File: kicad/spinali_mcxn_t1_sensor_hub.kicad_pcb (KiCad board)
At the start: 6 copper layers, 45 x 46 mm, 199 parts, among them J1 5055780421, J2 USB4105-GF-A, J3 CAN0A, J4 CAN0B, J5 Debug, J6 CAN1A, J7 CAN1B, J8 DF40TC(3.0)-50DP-0.4V(51), J9 DF40TC(3.0)-50DP-0.4V(51), Q1 BUK6D56-60EX, SW1 SW_SPST, U1 LM74700, U10 BMM350, U11 BMP581, U12 TJA1462ATK, U13 TJA1462ATK, U14 SK9822-EC20, U15 TJA1103AHN, U2 NX5P3363UKZ, U3 LM5160DNTJ, U4 NX5P3363UKZ, U5 MIC5504-1.8YMT, U6 MPM3811GG-Z, U7 MCXN947VDFT, U8 PCMF1USB3SZ, U9 ICM-45686, Y1 24MHz, Y2 32.768kHz, Y3 25MHz

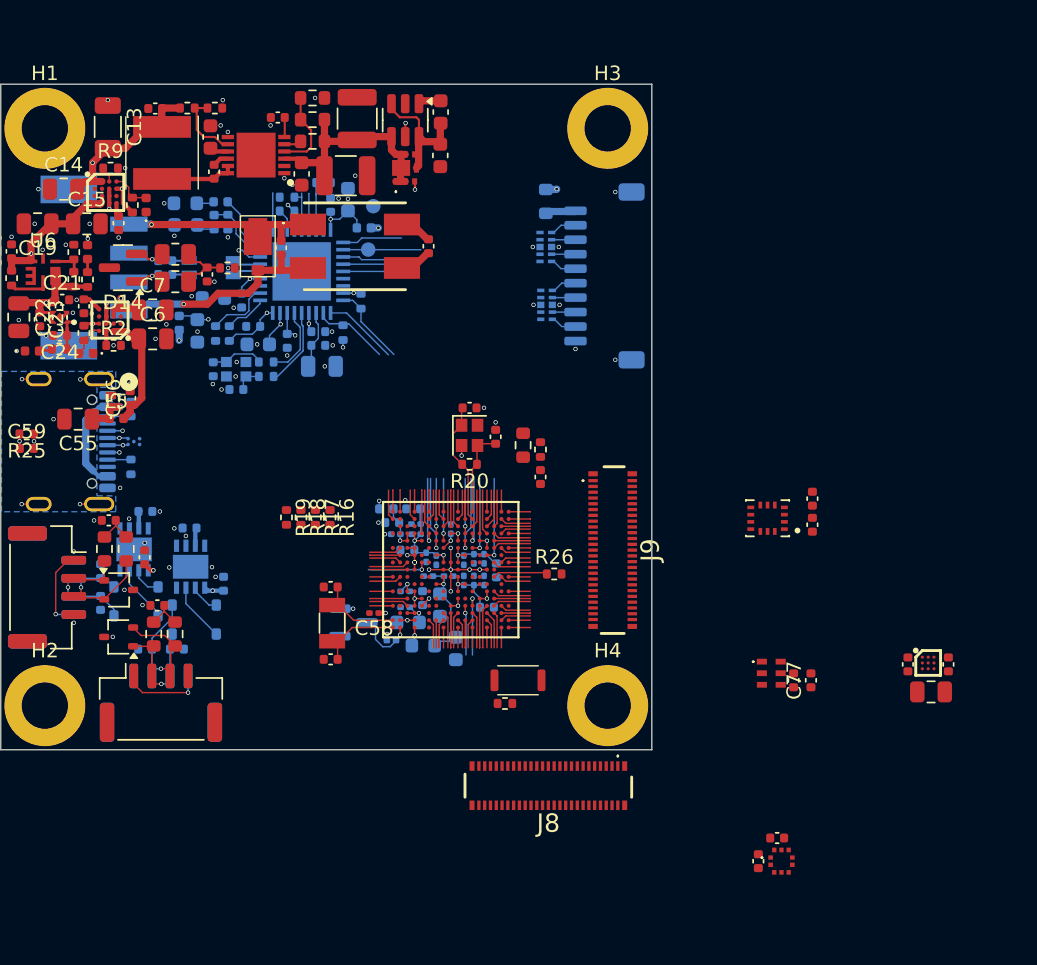
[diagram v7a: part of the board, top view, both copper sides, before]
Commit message: Updated PCB layout
Positioned MCXN947.
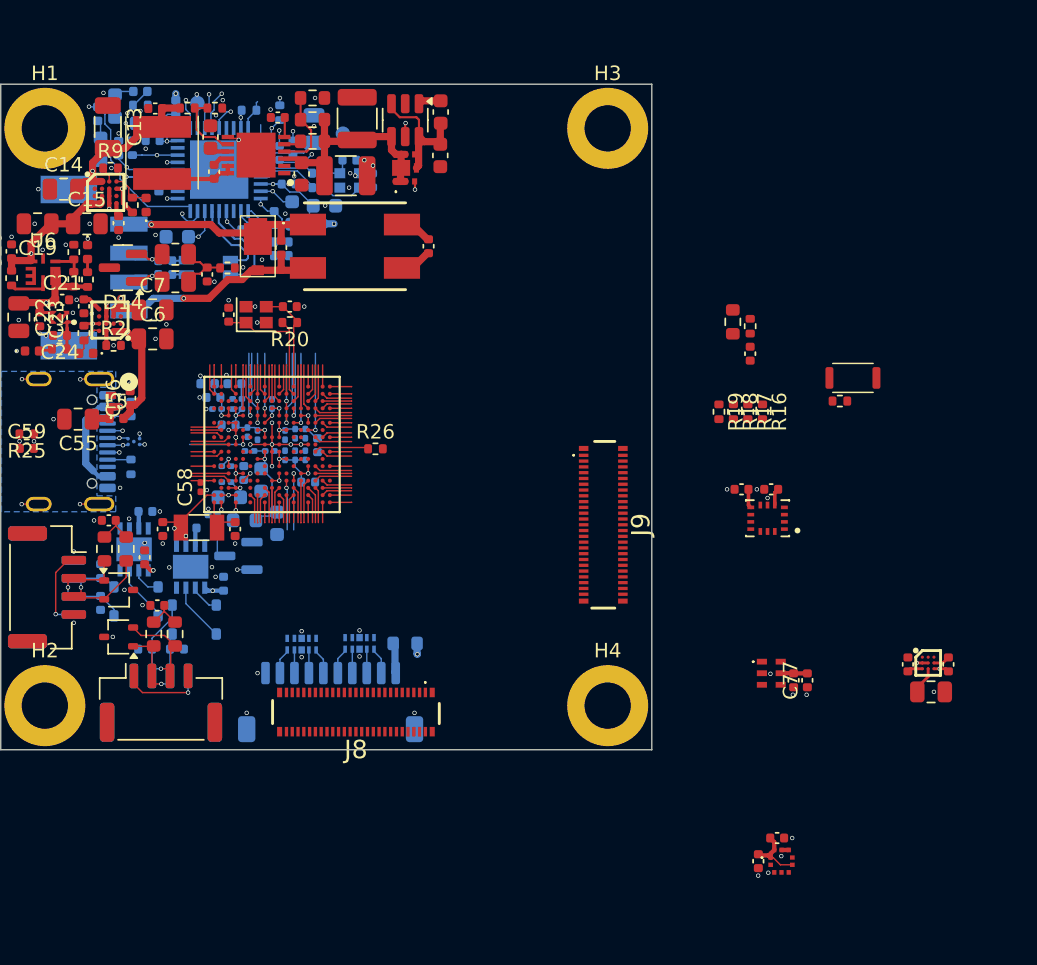
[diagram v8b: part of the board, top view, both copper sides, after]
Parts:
- moved J5 35.0 mm to (105.0, 118.7), turned to 180 degrees
- moved R29 32.1 mm to (110.1, 114.7), turned to 180 degrees
- moved SW1 31.2 mm to (141.1, 96.3)
- moved R15 31.2 mm to (140.2, 97.9)
- moved R16 30.8 mm to (134.8, 98.6)
- moved R17 30.8 mm to (133.8, 98.6)
- moved R18 30.8 mm to (132.8, 98.6)
- moved R19 30.8 mm to (131.8, 98.6)
- moved D8 30.3 mm to (107.0, 114.7), turned to 0 degrees
- moved D9 28.9 mm to (103.0, 114.7), turned to 0 degrees
- moved C26 17.9 mm to (97.9, 91.9), turned to -90 degrees
- moved C91 17.7 mm to (106.3, 81.2), turned to 0 degrees
- moved C90 17.1 mm to (107.9, 82.7), turned to 90 degrees
- moved Y1 16.9 mm to (99.8, 91.9), turned to 0 degrees
- moved C25 16.8 mm to (102.1, 91.4), turned to 180 degrees
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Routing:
- net VDDIO: track 25.9 -> 35.6 mm
- net Net-(U15-TMS/GPIO0/CONFIG0): track 4.66 -> 13.0 mm, vias 0 -> 2
- net Net-(U15-TDI/GPIO1): track 4.07 -> 12.2 mm, vias 0 -> 1
- net +3V3: track 37.5 -> 45.4 mm
- net GND: track 26.6 -> 32.1 mm, vias 97 -> 111
- net /Ethernet PHY/VDDA_AO: track 17.4 -> 12.1 mm, vias 3 -> 2
- net /Ethernet PHY/TRX_P: track 1.98 -> 7.03 mm
- net P1_20/ENET0_MDC: track 9.50 -> 5.40 mm
- net /Ethernet PHY/TRX_N: track 1.99 -> 5.86 mm
- net P1_7/ENET0_TXD1: track 6.74 -> 3.11 mm, vias 0 -> 1
- net P1_21/ENET0_MDIO: track 11.0 -> 7.56 mm
- net P1_4/ENET0_REFCLK: track 6.86 -> 3.85 mm, vias 0 -> 1
- net P1_19/ENET0_INT_N: track 10.7 -> 8.16 mm, vias 1 -> 2
- net P1_6/ENET0_TXD0: track 7.41 -> 4.84 mm, vias 0 -> 1
- net /MCU IO Part 2/P5_1/XTAL32K: track 6.00 -> 3.68 mm
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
